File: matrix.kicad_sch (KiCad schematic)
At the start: 132 parts, among them SW1 SW_Push, SW10 SW_Push, SW11 SW_Push, SW12 SW_Push, SW13 SW_Push, SW14 SW_Push, SW15 SW_Push, SW16 SW_Push, SW17 SW_Push, SW18 SW_Push, SW19 SW_Push, SW2 SW_Push, SW20 SW_Push, SW21 SW_Push, SW22 SW_Push, SW23 SW_Push, SW24 SW_Push, SW25 SW_Push, SW26 SW_Push, SW27 SW_Push, SW28 SW_Push, SW29 SW_Push, SW3 SW_Push, SW30 SW_Push, SW31 SW_Push, SW32 SW_Push, SW33 SW_Push, SW34 SW_Push, SW35 SW_Push, SW36 SW_Push, SW37 SW_Push, SW38 SW_Push, SW39 SW_Push, SW4 SW_Push, SW40 SW_Push, SW41 SW_Push, SW42 SW_Push, SW43 SW_Push, SW44 SW_Push, SW45 SW_Push, SW46 SW_Push, SW47 SW_Push, SW48 SW_Push, SW49 SW_Push, SW5 SW_Push, SW50 SW_Push, SW51 SW_Push, SW52 SW_Push, SW53 SW_Push, SW54 SW_Push, SW55 SW_Push, SW56 SW_Push, SW57 SW_Push, SW58 SW_Push, SW59 SW_Push, SW6 SW_Push, SW60 SW_Push, SW61 SW_Push, SW62 SW_Push, SW63 SW_Push, SW64 SW_Push, SW65 SW_Push, SW66 SW_Push, SW7 SW_Push, SW8 SW_Push, SW9 SW_Push

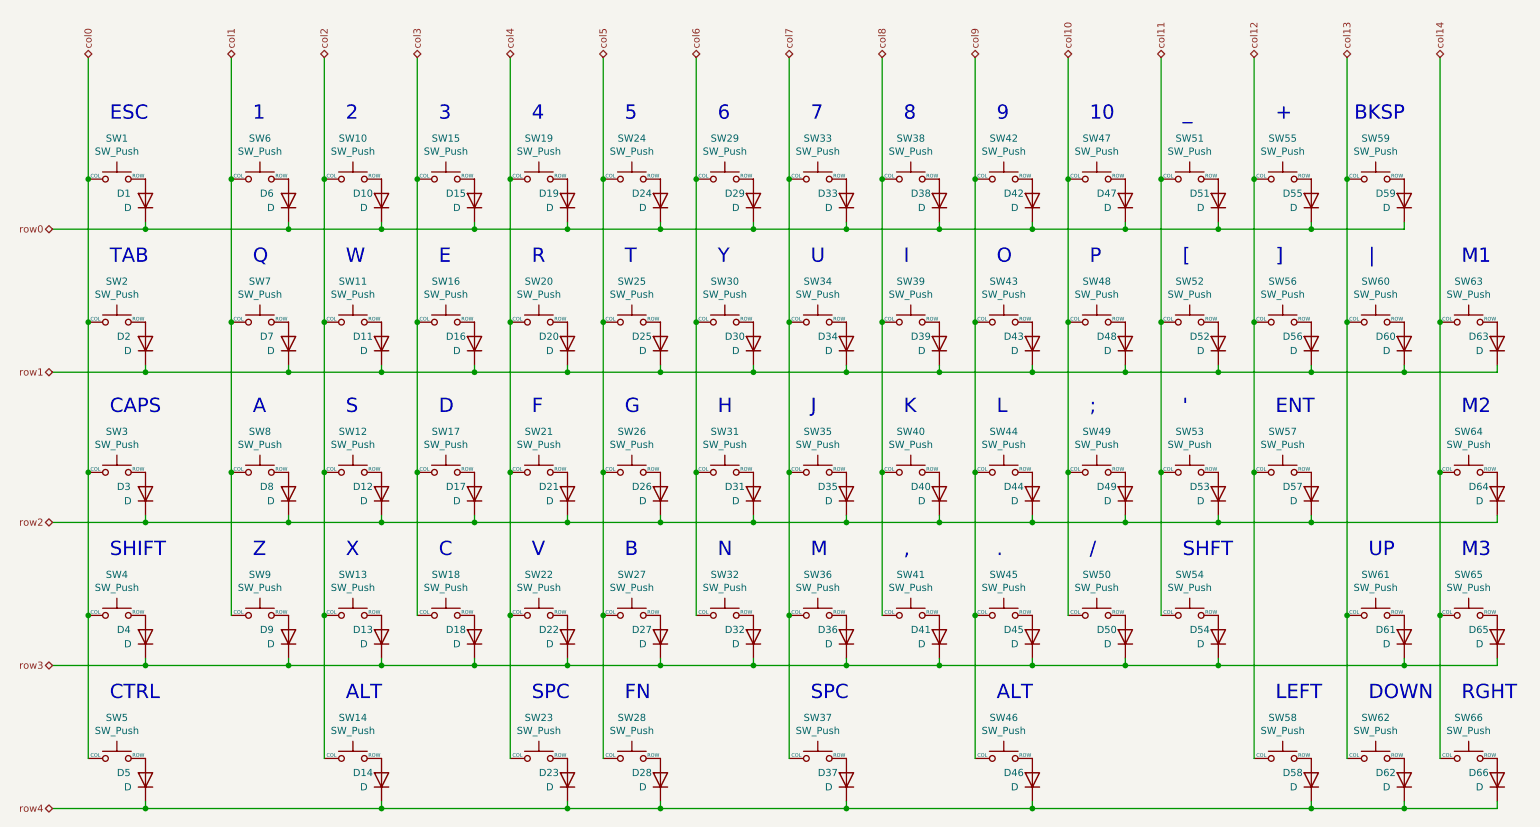
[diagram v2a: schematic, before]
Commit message: Added LGUI key
Community request to add a LGUI key to the board.
Added new key.
Rerouted.
Moved logos.
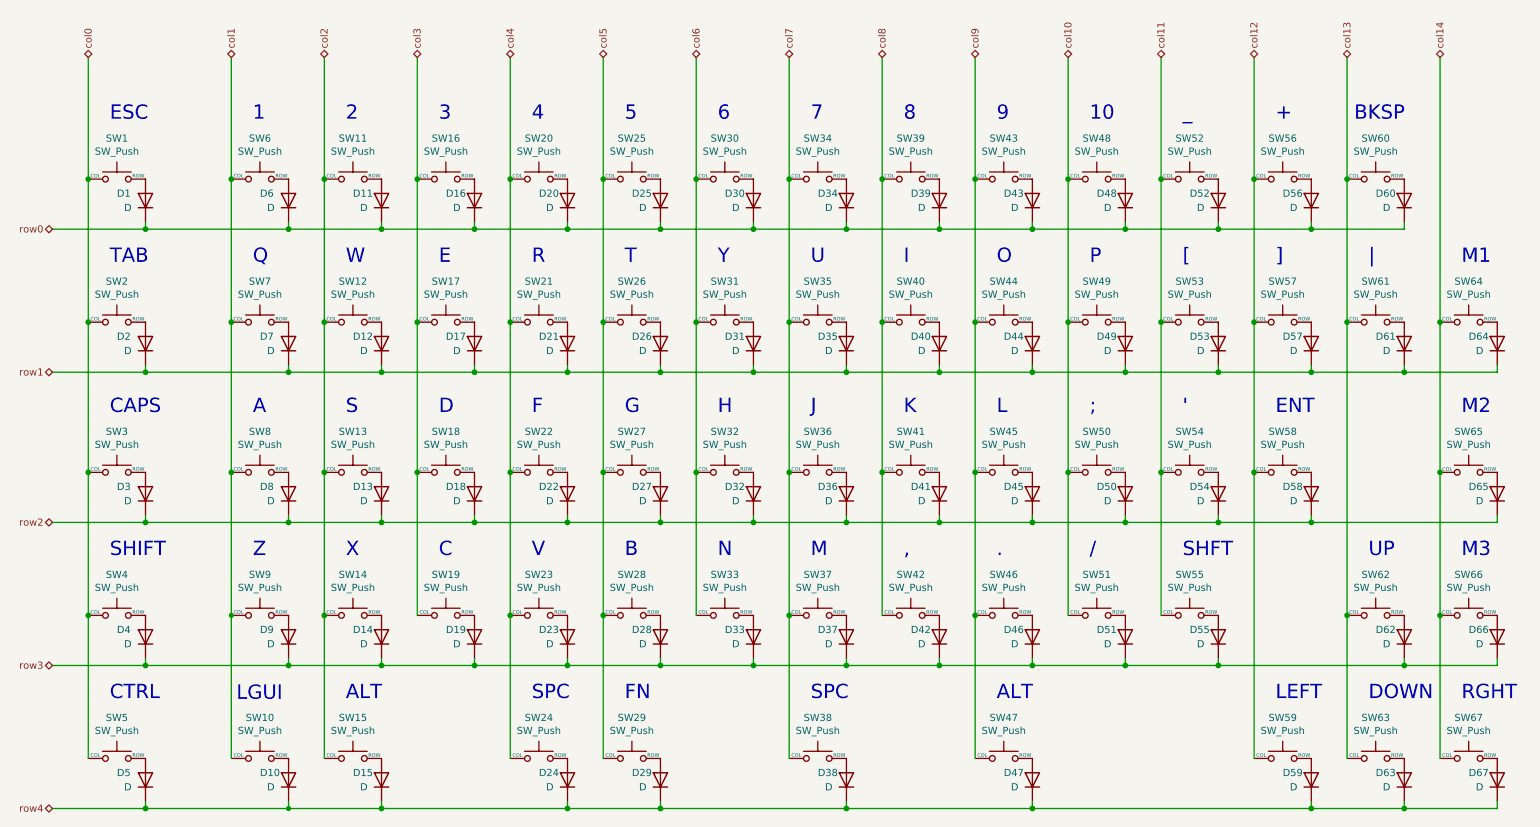
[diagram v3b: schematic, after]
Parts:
- added D10: D, arisutea:D_SOD-123, symbol arisutea-pcb:Device_D
- added SW10: SW_Push, arisutea:SW_Hotswap_Kailh_1.50u, symbol arisutea-pcb:Switch_SW_Keeb
- renumbered D10 to D11, D11 to D12, D12 to D13, D13 to D14, D14 to D15, D15 to D16, D16 to D17, D17 to D18, D18 to D19, D19 to D20, D20 to D21, D21 to D22, D22 to D23, D23 to D24, D24 to D25, D25 to D26, D26 to D27, D27 to D28, D28 to D29, D29 to D30, D30 to D31, D31 to D32, D32 to D33, D33 to D34, D34 to D35, D35 to D36, D36 to D37, D37 to D38, D38 to D39, D39 to D40, D40 to D41, D41 to D42, D42 to D43, D43 to D44, D44 to D45, D45 to D46, D46 to D47, D47 to D48, D48 to D49, D49 to D50, D50 to D51, D51 to D52, D52 to D53, D53 to D54, D54 to D55, D55 to D56, D56 to D57, D57 to D58, D58 to D59, D59 to D60, D60 to D61, D61 to D62, D62 to D63, D63 to D64, D64 to D65, D65 to D66, D66 to D67, SW10 to SW11, SW11 to SW12, SW12 to SW13, SW13 to SW14, SW14 to SW15, SW15 to SW16, SW16 to SW17, SW17 to SW18, SW18 to SW19, SW19 to SW20, SW20 to SW21, SW21 to SW22, SW22 to SW23, SW23 to SW24, SW24 to SW25, SW25 to SW26, SW26 to SW27, SW27 to SW28, SW28 to SW29, SW29 to SW30, SW30 to SW31, SW31 to SW32, SW32 to SW33, SW33 to SW34, SW34 to SW35, SW35 to SW36, SW36 to SW37, SW37 to SW38, SW38 to SW39, SW39 to SW40, SW40 to SW41, SW41 to SW42, SW42 to SW43, SW43 to SW44, SW44 to SW45, SW45 to SW46, SW46 to SW47, SW47 to SW48, SW48 to SW49, SW49 to SW50, SW50 to SW51, SW51 to SW52, SW52 to SW53, SW53 to SW54, SW54 to SW55, SW55 to SW56, SW56 to SW57, SW57 to SW58, SW58 to SW59, SW59 to SW60, SW60 to SW61, SW61 to SW62, SW62 to SW63, SW63 to SW64, SW64 to SW65, SW65 to SW66, SW66 to SW67
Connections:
- net col1: now also SW10.1 (COL)
- net row4: now also D10.1 (K)
- new net: D10.2 (A), SW10.2 (ROW)
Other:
- note added: "LGUI"
